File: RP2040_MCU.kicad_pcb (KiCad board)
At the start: 2 copper layers, 36 parts, among them J1 USB_C_Receptacle_USB2.0, J2 Conn_01x18, J3 Conn_01x18, SW1 SW_Push, SW2 SW_Push, U1 W25Q128JVS, U2 USBLC6-2SC6, U3 RP2040, U4 XC6206PxxxMR, Y1 Crystal_GND23

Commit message: finished routing
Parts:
- moved J2 1.79 mm to (123.2, 22.3)
- moved C16 1.50 mm to (130.4, 56.5)
- moved J3 1.19 mm to (155.2, 22.3)
- moved C2 0.46 mm to (129.0, 63.8)
- moved C7 0.35 mm to (141.6, 47.0)
- moved C10 0.31 mm to (143.8, 47.0)
- moved C12 0.19 mm to (146.1, 52.2)
- moved C9 0.11 mm to (137.0, 47.1)
- moved C5 0.06 mm to (134.8, 47.0)
- moved C8 0.06 mm to (139.1, 47.1)
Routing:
- net +3V3: track 75.2 -> 184.4 mm, vias 3 -> 8
- net GND: track 0.00 -> 51.9 mm, vias 0 -> 128
- net /GPIO23: track 6.46 -> 24.9 mm
- net unconnected-(J1-PadS1): track 0.00 -> 17.0 mm
- net /GPIO21: track 7.23 -> 23.4 mm
- net /GPIO22: track 7.46 -> 22.9 mm
- net /GPIO20: track 8.01 -> 21.4 mm
- net SWD: track 6.85 -> 18.0 mm
- net /GPIO19: track 8.21 -> 19.3 mm
- net /GPIO18: track 6.63 -> 16.9 mm
- net +1V1: track 16.3 -> 26.5 mm, vias 0 -> 2
- net /GPIO17: track 6.32 -> 16.5 mm
- net /GPIO16: track 6.10 -> 15.9 mm
- net SWCLK: track 10.9 -> 18.7 mm
- net /GPIO24: track 30.8 -> 27.0 mm
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- added copper zone on B.Cu, net GND
- added copper zone on F.Cu, net GND
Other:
- board outline added: 37.4 x 48.1 mm

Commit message: Finished Board. Need to double check and review
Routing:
- net GND: track 51.9 -> 66.5 mm, vias 128 -> 83
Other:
- board size 37.4 x 48.1 mm -> 38 x 48.5 mm

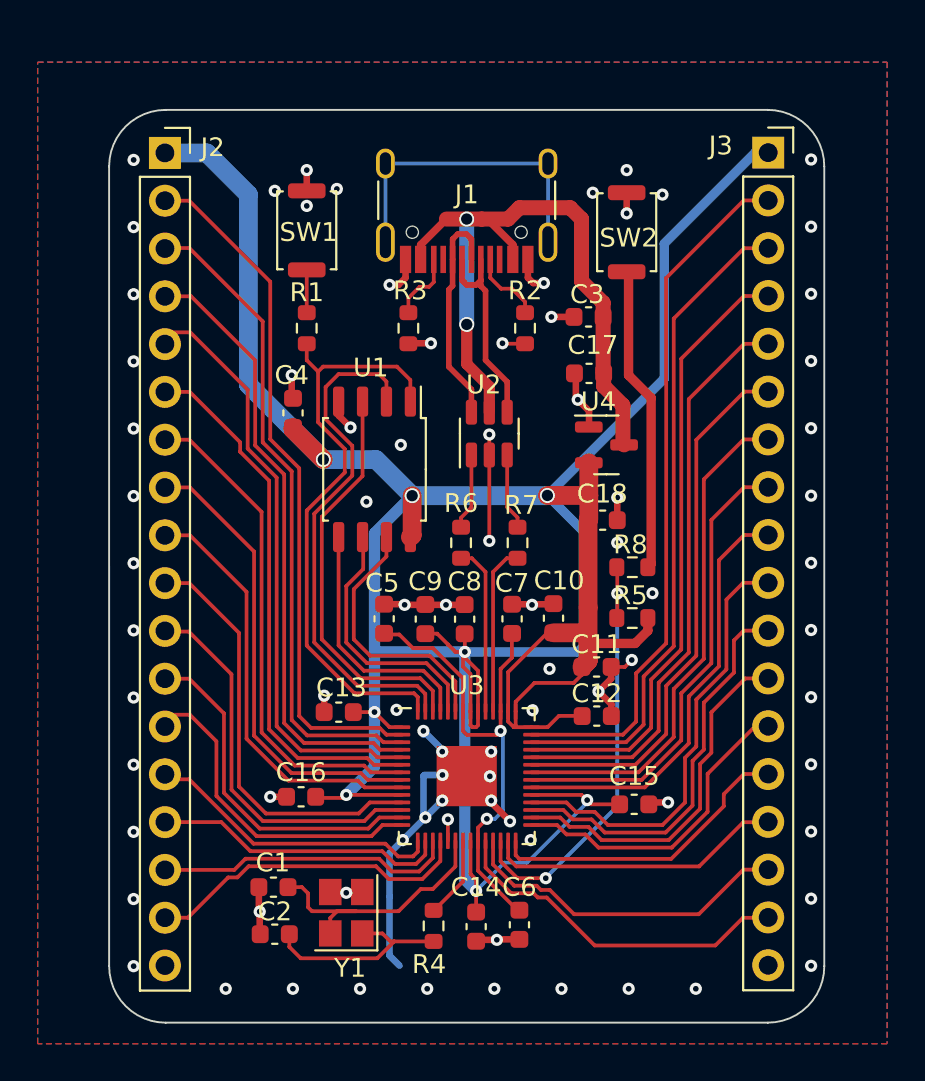
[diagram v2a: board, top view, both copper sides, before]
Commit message: fixed gpio traces
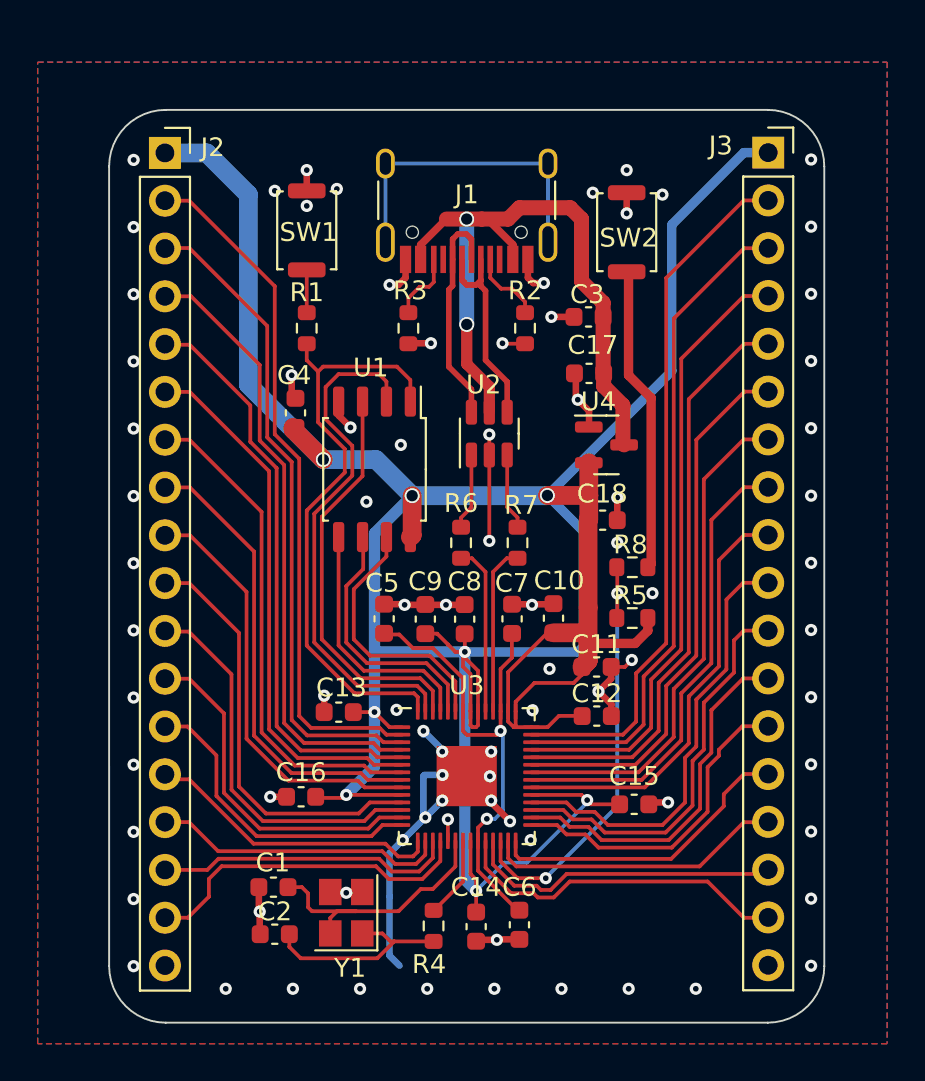
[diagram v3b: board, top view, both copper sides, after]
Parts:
- moved C4 0.13 mm to (130.1, 36.1)
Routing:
- net SWD: track 18.0 -> 16.9 mm
- net /GPIO3: track 31.5 -> 30.8 mm
- net /GPIO11: track 17.2 -> 16.5 mm
- net /GPIO15: track 17.5 -> 18.1 mm
- net SWCLK: track 18.7 -> 18.2 mm
